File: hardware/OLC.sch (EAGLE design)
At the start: 12 parts, among them IC1 MCP23017SP, J1 61301011121

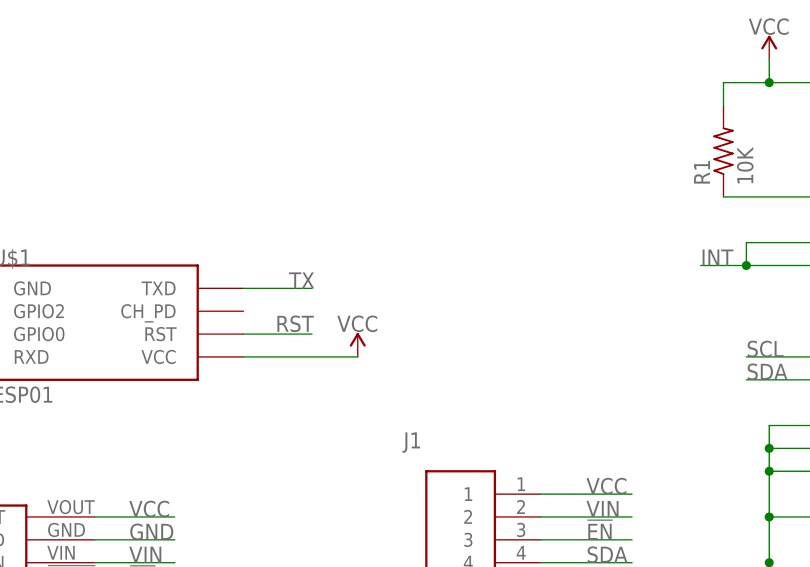
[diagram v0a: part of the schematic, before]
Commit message: Add 5K ohm resistor as R3
The ESP01 needs a pull-up resistor on CH_PD to boot, and previous designs were missing it.
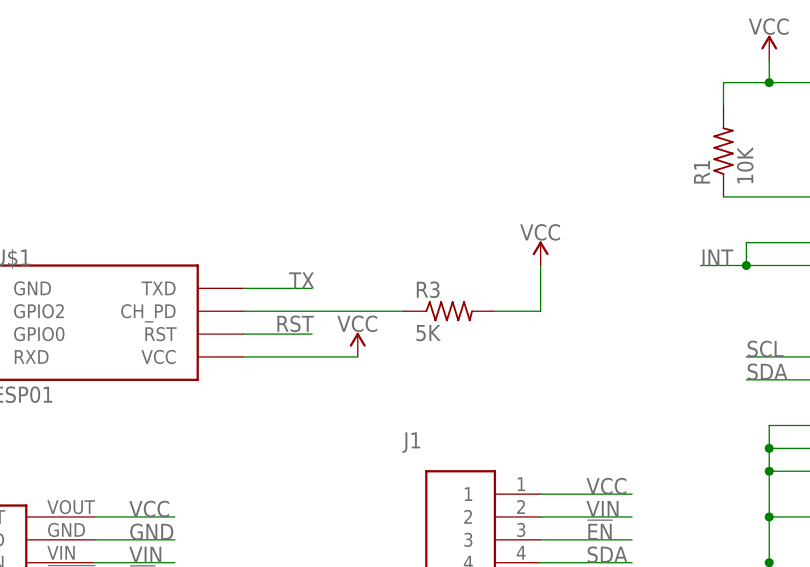
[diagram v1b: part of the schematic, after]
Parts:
- added R3: 5K, resistor:R-US_0207/10
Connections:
- new net N$11: R3.1, U$1.CH_PD
- net VCC: now also R3.2
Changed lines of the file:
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@@
 <grid distance="0.1" unitdist="inch" unit="inch" style="lines" multiple="1" display="no" altdistance="0.01" altunitdist="inch" altunit="inch"/>
 <layers>
-<layer number="1" name="Top" color="4" fill="1" visible="no" active="no"/>
-<layer number="2" name="Route2" color="16" fill="1" visible="no" active="no"/>
-<layer number="3" name="Route3" color="17" fill="1" visible="no" active="no"/>
-<layer number="4" name="Route4" color="18" fill="1" visible="no" active="no"/>
-<layer number="5" name="Route5" color="19" fill="1" visible="no" active="no"/>
-<layer number="6" name="Route6" color="25" fill="1" visible="no" active="no"/>
-<layer number="7" name="Route7" color="26" fill="1" visible="no" active="no"/>
-<layer number="8" name="Route8" color="27" fill="1" visible="no" active="no"/>
-<layer number="9" name="Route9" color="28" fill="1" visible="no" active="no"/>
-<layer number="10" name="Route10" color="29" fill="1" visible="no" active="no"/>
-<layer number="11" name="Route11" color="30" fill="1" visible="no" active="no"/>
-<layer number="12" name="Route12" color="20" fill="1" visible="no" active="no"/>
-<layer number="13" name="Route13" color="21" fill="1" visible="no" active="no"/>
-<layer number="14" name="Route14" color="22" fill="1" visible="no" active="no"/>
-<layer number="15" name="Route15" color="23" fill="1" visible="no" active="no"/>
-<layer number="16" name="Bottom" color="1" fill="1" visible="no" active="no"/>
-<layer number="17" name="Pads" color="2" fill="1" visible="no" active="no"/>
-<layer number="18" name="Vias" color="2" fill="1" visible="no" active="no"/>
-<layer number="19" name="Unrouted" color="6" fill="1" visible="no" active="no"/>
-<layer number="20" name="Dimension" color="24" fill="1" visible="no" active="no"/>
-<layer number="21" name="tPlace" color="7" fill="1" visible="no" active="no"/>
-<layer number="22" name="bPlace" color="7" fill="1" visible="no" active="no"/>
-<layer number="23" name="tOrigins" color="15" fill="1" visible="no" active="no"/>
-<layer number="24" name="bOrigins" color="15" fill="1" visible="no" active="no"/>
-<layer number="25" name="tNames" color="7" fill="1" visible="no" active="no"/>
-<layer number="26" name="bNames" color="7" fill="1" visible="no" active="no"/>
-<layer number="27" name="tValues" color="7" fill="1" visible="no" active="no"/>
-<layer number="28" name="bValues" color="7" fill="1" visible="no" active="no"/>
+<layer number="1" name="Top" color="4" fill="1" visible="yes" active="no"/>
+<layer number="2" name="Route2" color="16" fill="1" visible="yes" active="no"/>
+<layer number="3" name="Route3" color="17" fill="1" visible="yes" active="no"/>
+<layer number="4" name="Route4" color="18" fill="1" visible="yes" active="no"/>
+<layer number="5" name="Route5" color="19" fill="1" visible="yes" active="no"/>
+<layer number="6" name="Route6" color="25" fill="1" visible="yes" active="no"/>
+<layer number="7" name="Route7" color="26" fill="1" visible="yes" active="no"/>
+<layer number="8" name="Route8" color="27" fill="1" visible="yes" active="no"/>
+<layer number="9" name="Route9" color="28" fill="1" visible="yes" active="no"/>
+<layer number="10" name="Route10" color="29" fill="1" visible="yes" active="no"/>
+<layer number="11" name="Route11" color="30" fill="1" visible="yes" active="no"/>
+<layer number="12" name="Route12" color="20" fill="1" visible="yes" active="no"/>
+<layer number="13" name="Route13" color="21" fill="1" visible="yes" active="no"/>
+<layer number="14" name="Route14" color="22" fill="1" visible="yes" active="no"/>
+<layer number="15" name="Route15" color="23" fill="1" visible="yes" active="no"/>
+<layer number="16" name="Bottom" color="1" fill="1" visible="yes" active="no"/>
+<layer number="17" name="Pads" color="2" fill="1" visible="yes" active="no"/>
+<layer number="18" name="Vias" color="2" fill="1" visible="yes" active="no"/>
+<layer number="19" name="Unrouted" color="6" fill="1" visible="yes" active="no"/>
+<layer number="20" name="Dimension" color="24" fill="1" visible="yes" active="no"/>
+<layer number="21" name="tPlace" color="7" fill="1" visible="yes" active="no"/>
+<layer number="22" name="bPlace" color="7" fill="1" visible="yes" active="no"/>
+<layer number="23" name="tOrigins" color="15" fill="1" visible="yes" active="no"/>
+<layer number="24" name="bOrigins" color="15" fill="1" visible="yes" active="no"/>
+<layer number="25" name="tNames" color="7" fill="1" visible="yes" active="no"/>
+<layer number="26" name="bNames" color="7" fill="1" visible="yes" active="no"/>
+<layer number="27" name="tValues" color="7" fill="1" visible="yes" active="no"/>
+<layer number="28" name="bValues" color="7" fill="1" visible="yes" active="no"/>
 <layer number="29" name="tStop" color="7" fill="3" visible="no" active="no"/>
 <layer number="30" name="bStop" color="7" fill="6" visible="no" active="no"/>
@@
 <layer number="35" name="tGlue" color="7" fill="4" visible="no" active="no"/>
 <layer number="36" name="bGlue" color="7" fill="5" visible="no" active="no"/>
-<layer number="37" name="tTest" color="7" fill="1" visible="no" active="no"/>
-<layer number="38" name="bTest" color="7" fill="1" visible="no" active="no"/>
+<layer number="37" name="tTest" color="7" fill="1" visible="yes" active="no"/>
+<layer number="38" name="bTest" color="7" fill="1" visible="yes" active="no"/>
 <layer number="39" name="tKeepout" color="4" fill="11" visible="no" active="no"/>
 <layer number="40" name="bKeepout" color="1" fill="11" visible="no" active="no"/>
@@
 <layer number="44" name="Drills" color="7" fill="1" visible="no" active="no"/>
 <layer number="45" name="Holes" color="7" fill="1" visible="no" active="no"/>
-<layer number="46" name="Milling" color="3" fill="1" visible="no" active="no"/>
-<layer number="47" name="Measures" color="7" fill="1" visible="no" active="no"/>
-<layer number="48" name="Document" color="7" fill="1" visible="no" active="no"/>
-<layer number="49" name="Reference" color="7" fill="1" visible="no" active="no"/>
-<layer number="50" name="dxf" color="7" fill="1" visible="no" active="no"/>
-<layer number="51" name="tDocu" color="7" fill="1" visible="no" active="no"/>
-<layer number="52" name="bDocu" color="7" fill="1" visible="no" active="no"/>
-<layer number="53" name="tGND_GNDA" color="7" fill="9" visible="no" active="no"/>
-<layer number="54" name="bGND_GNDA" color="1" fill="9" visible="no" active="no"/>
-<layer number="56" name="wert" color="7" fill="1" visible="no" active="no"/>
-<layer number="57" name="tCAD" color="7" fill="1" visible="no" active="no"/>
-<layer number="59" name="tCarbon" color="7" fill="1" visible="no" active="no"/>
-<layer number="60" name="bCarbon" color="7" fill="1" visible="no" active="no"/>
+<layer number="46" name="Milling" color="3" fill="1" visible="yes" active="no"/>
+<layer number="47" name="Measures" color="7" fill="1" visible="yes" active="no"/>
+<layer number="48" name="Document" color="7" fill="1" visible="yes" active="no"/>
+<layer number="49" name="Reference" color="7" fill="1" visible="yes" active="no"/>
+<layer number="50" name="dxf" color="7" fill="1" visible="yes" active="no"/>
+<layer number="51" name="tDocu" color="7" fill="1" visible="yes" active="no"/>
+<layer number="52" name="bDocu" color="7" fill="1" visible="yes" active="no"/>
+<layer number="53" name="tGND_GNDA" color="7" fill="9" visible="yes" active="no"/>
+<layer number="54" name="bGND_GNDA" color="1" fill="9" visible="yes" active="no"/>
+<layer number="56" name="wert" color="7" fill="1" visible="yes" active="no"/>
+<layer number="57" name="tCAD" color="7" fill="1" visible="yes" active="no"/>
+<layer number="59" name="tCarbon" color="7" fill="1" visible="yes" active="no"/>
+<layer number="60" name="bCarbon" color="7" fill="1" visible="yes" active="no"/>
 <layer number="88" name="SimResults" color="9" fill="1" visible="yes" active="yes"/>
 <layer number="89" name="SimProbes" color="9" fill="1" visible="yes" active="yes"/>
@@
 <part name="VR2" library="Custom Parts" deviceset="D24V10" device=""/>
 <part name="J2" library="SparkFun-Connectors" library_urn="urn:adsk.eagle:library:513" deviceset="CONN_02" device="3.5MM" package3d_urn="urn:adsk.eagle:package:38050/1"/>
+<part name="R3" library="resistor" library_urn="urn:adsk.eagle:library:348" deviceset="R-US_" device="0207/10" package3d_urn="urn:adsk.eagle:package:23491/2" value="5K"/>
+<part name="SUPPLY3" library="SparkFun-PowerSymbols" library_urn="urn:adsk.eagle:library:530" deviceset="VCC" device=""/>
 </parts>
 <sheets>
@@
 <attribute name="VALUE" x="-33.02" y="51.054" size="1.778" layer="96" font="vector"/>
 <attribute name="NAME" x="-33.02" y="61.468" size="1.778" layer="95" font="vector"/>
+</instance>
+<instance part="R3" gate="G$1" x="27.94" y="144.78" smashed="yes">
+<attribute name="NAME" x="24.13" y="146.2786" size="1.778" layer="95"/>
+<attribute name="VALUE" x="24.13" y="141.478" size="1.778" layer="96"/>
+</instance>
+<instance part="SUPPLY3" gate="G$1" x="38.1" y="149.86" smashed="yes">
+<attribute name="VALUE" x="38.1" y="152.654" size="1.778" layer="96" align="bottom-center"/>
 </instance>
 </instances>
@@
 <label x="-7.62" y="121.92" size="1.778" layer="95" font="vector"/>
 </segment>
+<segment>
+<pinref part="R3" gate="G$1" pin="2"/>
+<wire x1="33.02" y1="144.78" x2="38.1" y2="144.78" width="0.1524" layer="91"/>
+<wire x1="38.1" y1="144.78" x2="38.1" y2="149.86" width="0.1524" layer="91"/>
+<pinref part="SUPPLY3" gate="G$1" pin="VCC"/>
+</segment>
 </net>
 <net name="PIR1" class="0">
@@
 </segment>
 </net>
+<net name="N$11" class="0">
+<segment>
+<pinref part="U$1" gate="G$1" pin="CH_PD"/>
+<pinref part="R3" gate="G$1" pin="1"/>
+<wire x1="5.08" y1="144.78" x2="22.86" y2="144.78" width="0.1524" layer="91"/>
+</segment>
+</net>
